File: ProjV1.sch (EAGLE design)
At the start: 24 parts, among them IC1 CD4007UBM, IC2 CD4007UBM, IC3 CD4007UBM, SW1 EC12E_SW, U1 MIC5504-3.3YM5-T5, U2 MCP2200-I/SS, U3 ATMEGA328PB-AU, Y1 12MHz

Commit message: Updated schematic and pdf
Switched serial chip to run on 3.3V and  updated the pdf file
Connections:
- removed net N$11: C1.2, U2.VSS
- removed net N$21: C1.1, U2.VUSB
- net +5V: no longer U2.VDD
- net 0: now also C1.2
- net VCC: now also C1.1, U2.VDD, U2.VUSB
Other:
- moved on the sheet: C1
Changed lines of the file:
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@@
 <part name="X_10" library="ngspice-simulation" library_urn="urn:adsk.eagle:library:527439" deviceset="GND" device=""/>
 <part name="P+6" library="supply1" library_urn="urn:adsk.eagle:library:371" deviceset="+5V" device=""/>
-<part name="P+7" library="supply1" library_urn="urn:adsk.eagle:library:371" deviceset="+5V" device=""/>
 <part name="P+8" library="supply1" library_urn="urn:adsk.eagle:library:371" deviceset="+5V" device=""/>
+<part name="X_11" library="ngspice-simulation" library_urn="urn:adsk.eagle:library:527439" deviceset="GND" device=""/>
+<part name="P+7" library="supply1" library_urn="urn:adsk.eagle:library:371" deviceset="VCC" device=""/>
 </parts>
 <sheets>
@@
 <instance part="X_2" gate="G$1" x="-241.3" y="337.82" smashed="yes"/>
 <instance part="X_3" gate="G$1" x="-226.06" y="261.62" smashed="yes"/>
-<instance part="C1" gate="G$1" x="-139.7" y="243.84" smashed="yes">
-<attribute name="NAME" x="-138.684" y="244.475" size="1.778" layer="95"/>
-<attribute name="VALUE" x="-138.684" y="239.649" size="1.778" layer="96"/>
+<instance part="C1" gate="G$1" x="-139.7" y="256.54" smashed="yes">
+<attribute name="NAME" x="-138.684" y="257.175" size="1.778" layer="95"/>
+<attribute name="VALUE" x="-138.684" y="252.349" size="1.778" layer="96"/>
 </instance>
 <instance part="X_4" gate="G$1" x="-71.12" y="223.52" smashed="yes"/>
@@
 <attribute name="VALUE" x="-231.14" y="355.6" size="1.778" layer="96" rot="R90"/>
 </instance>
-<instance part="P+7" gate="1" x="-139.7" y="271.78" smashed="yes">
-<attribute name="VALUE" x="-142.24" y="266.7" size="1.778" layer="96" rot="R90"/>
-</instance>
 <instance part="P+8" gate="1" x="-256.54" y="327.66" smashed="yes">
 <attribute name="VALUE" x="-259.08" y="322.58" size="1.778" layer="96" rot="R90"/>
+</instance>
+<instance part="X_11" gate="G$1" x="-139.7" y="246.38" smashed="yes"/>
+<instance part="P+7" gate="VCC" x="-139.7" y="271.78" smashed="yes">
+<attribute name="VALUE" x="-142.24" y="269.24" size="1.778" layer="96" rot="R90"/>
 </instance>
 </instances>
@@
 <junction x="-175.26" y="325.12"/>
 </segment>
-</net>
-<net name="N$21" class="0">
-<segment>
-<pinref part="U2" gate="G$1" pin="VUSB"/>
-<wire x1="-132.08" y1="261.62" x2="-139.7" y2="261.62" width="0.1524" layer="91"/>
-<pinref part="C1" gate="G$1" pin="1"/>
-<wire x1="-139.7" y1="261.62" x2="-139.7" y2="246.38" width="0.1524" layer="91"/>
+<segment>
+<pinref part="X_11" gate="G$1" pin="0"/>
+<pinref part="C1" gate="G$1" pin="2"/>
+<wire x1="-139.7" y1="246.38" x2="-139.7" y2="251.46" width="0.1524" layer="91"/>
 </segment>
 </net>
@@
 <pinref part="U$1" gate="G$1" pin="VCC"/>
 <wire x1="-63.5" y1="231.14" x2="-71.12" y2="231.14" width="0.1524" layer="91"/>
+</segment>
+<segment>
+<pinref part="U2" gate="G$1" pin="VDD"/>
+<wire x1="-132.08" y1="264.16" x2="-139.7" y2="264.16" width="0.1524" layer="91"/>
+<label x="-139.7" y="264.16" size="1.778" layer="95"/>
+<wire x1="-139.7" y1="269.24" x2="-139.7" y2="264.16" width="0.1524" layer="91"/>
+<pinref part="P+7" gate="VCC" pin="VCC"/>
+<pinref part="U2" gate="G$1" pin="VUSB"/>
+<wire x1="-132.08" y1="261.62" x2="-139.7" y2="261.62" width="0.1524" layer="91"/>
+<pinref part="C1" gate="G$1" pin="1"/>
+<wire x1="-139.7" y1="261.62" x2="-139.7" y2="259.08" width="0.1524" layer="91"/>
+<wire x1="-139.7" y1="264.16" x2="-139.7" y2="261.62" width="0.1524" layer="91"/>
+<junction x="-139.7" y="264.16"/>
+<junction x="-139.7" y="261.62"/>
 </segment>
 </net>
@@
 </segment>
 </net>
-<net name="N$11" class="0">
-<segment>
-<pinref part="U2" gate="G$1" pin="VSS"/>
-<wire x1="-132.08" y1="223.52" x2="-139.7" y2="223.52" width="0.1524" layer="91"/>
-<pinref part="C1" gate="G$1" pin="2"/>
-<wire x1="-139.7" y1="238.76" x2="-139.7" y2="223.52" width="0.1524" layer="91"/>
-</segment>
-</net>
 <net name="N$30" class="0">
 <segment>
@@
 </segment>
 <segment>
-<pinref part="U2" gate="G$1" pin="VDD"/>
-<wire x1="-132.08" y1="264.16" x2="-139.7" y2="264.16" width="0.1524" layer="91"/>
-<label x="-139.7" y="264.16" size="1.778" layer="95"/>
-<pinref part="P+7" gate="1" pin="+5V"/>
-<wire x1="-139.7" y1="269.24" x2="-139.7" y2="264.16" width="0.1524" layer="91"/>
-</segment>
-<segment>

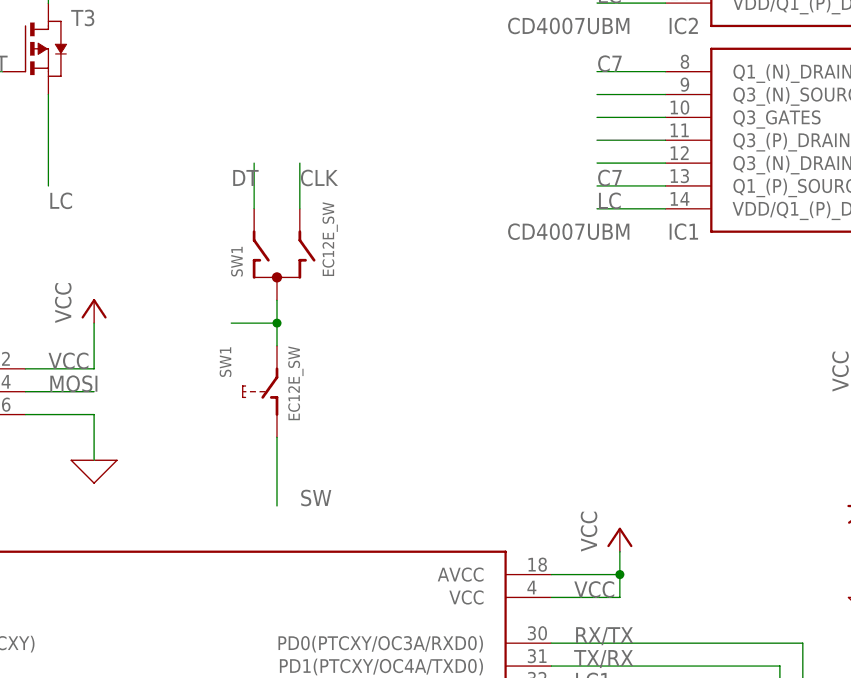
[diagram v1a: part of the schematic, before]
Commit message: Updated Board Layout and Cam filse
Rerouted wires to make board smaller
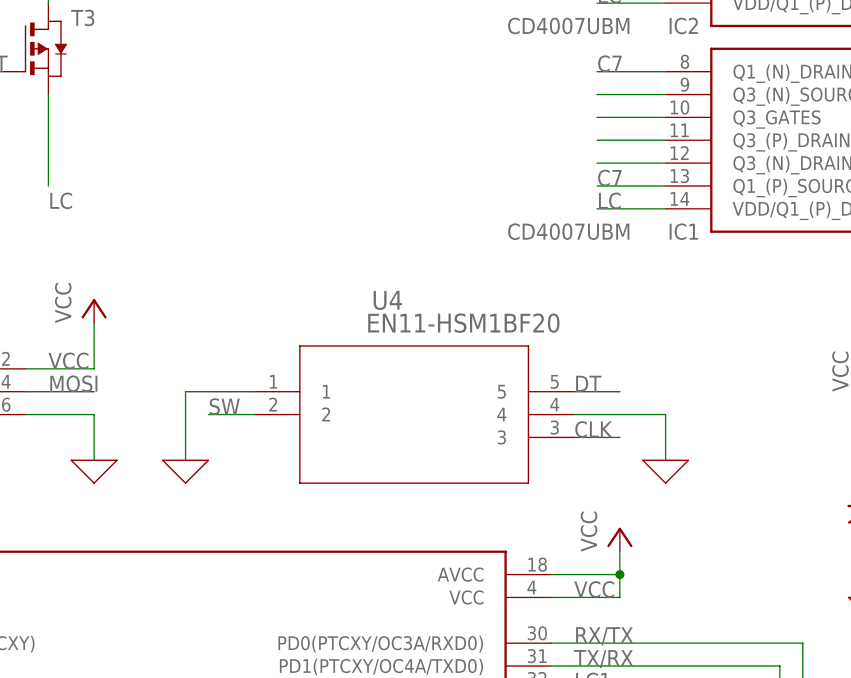
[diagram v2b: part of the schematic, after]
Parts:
- removed SW1: EC12E_SW, switch-alps:EC12E_SW
- added U4: EN11-HSM1BF20, EN11-HSM1BF20:EN11-HSM1BF20
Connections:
- removed net N$7: SW1G$1.C, SW1G$2.2
- net 0: now also U4.1, U4.4
- net CLK: now also U4.3; no longer SW1G$1.B
- net DT: now also U4.5; no longer SW1G$1.A
- net SW: now also U4.2; no longer SW1G$2.1
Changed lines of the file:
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@@
 <part name="LED4" library="led" library_urn="urn:adsk.eagle:library:259" deviceset="LED" device="CHIP-LED0805" package3d_urn="urn:adsk.eagle:package:15818/2"/>
 <part name="LED5" library="led" library_urn="urn:adsk.eagle:library:259" deviceset="LED" device="CHIP-LED0805" package3d_urn="urn:adsk.eagle:package:15818/2"/>
-<part name="SW1" library="switch-alps" library_urn="urn:adsk.eagle:library:373" deviceset="EC12E_SW" device="" package3d_urn="urn:adsk.eagle:package:27083/1"/>
 <part name="Y1" library="SparkFun-Clocks" deviceset="RESONATOR-16MHZ" device="SMD_3.2X1.3" value="12MHz"/>
 <part name="X_1" library="ngspice-simulation" library_urn="urn:adsk.eagle:library:527439" deviceset="GND" device=""/>
@@
 <part name="X_11" library="ngspice-simulation" library_urn="urn:adsk.eagle:library:527439" deviceset="GND" device=""/>
 <part name="P+7" library="supply1" library_urn="urn:adsk.eagle:library:371" deviceset="VCC" device=""/>
+<part name="U4" library="EN11-HSM1BF20" deviceset="EN11-HSM1BF20" device=""/>
+<part name="X_12" library="ngspice-simulation" library_urn="urn:adsk.eagle:library:527439" deviceset="GND" device=""/>
+<part name="X_13" library="ngspice-simulation" library_urn="urn:adsk.eagle:library:527439" deviceset="GND" device=""/>
 </parts>
 <sheets>
@@
 <attribute name="VALUE" x="-41.148" y="318.135" size="1.778" layer="96" rot="R180"/>
 </instance>
-<instance part="SW1" gate="G$1" x="-205.74" y="281.94" smashed="yes">
-<attribute name="PART" x="-209.55" y="281.94" size="1.27" layer="95" rot="R90"/>
-<attribute name="VALUE" x="-199.39" y="281.94" size="1.27" layer="96" rot="R90"/>
-</instance>
-<instance part="SW1" gate="G$2" x="-205.74" y="269.24" smashed="yes" rot="MR270">
-<attribute name="PART" x="-210.82" y="274.32" size="1.27" layer="95" rot="MR270"/>
-<attribute name="VALUE" x="-203.2" y="274.32" size="1.27" layer="96" rot="MR270"/>
-</instance>
 <instance part="Y1" gate="G$1" x="-83.82" y="251.46" smashed="yes" rot="MR270">
 <attribute name="NAME" x="-81.28" y="254.762" size="1.778" layer="95" font="vector" rot="MR270" align="center-right"/>
@@
 <attribute name="VALUE" x="-142.24" y="269.24" size="1.778" layer="96" rot="R90"/>
 </instance>
+<instance part="U4" gate="A" x="-210.82" y="269.24" smashed="yes">
+<attribute name="NAME" x="-195.2244" y="278.3586" size="2.0828" layer="95" ratio="6" rot="SR0"/>
+<attribute name="VALUE" x="-195.8594" y="275.8186" size="2.0828" layer="96" ratio="6" rot="SR0"/>
+</instance>
+<instance part="X_12" gate="G$1" x="-162.56" y="261.62" smashed="yes"/>
+<instance part="X_13" gate="G$1" x="-215.9" y="261.62" smashed="yes"/>
 </instances>
 <busses>
@@
 <wire x1="-139.7" y1="246.38" x2="-139.7" y2="251.46" width="0.1524" layer="91"/>
 </segment>
+<segment>
+<pinref part="X_12" gate="G$1" pin="0"/>
+<wire x1="-162.56" y1="261.62" x2="-162.56" y2="266.7" width="0.1524" layer="91"/>
+<pinref part="U4" gate="A" pin="4"/>
+<wire x1="-162.56" y1="266.7" x2="-172.72" y2="266.7" width="0.1524" layer="91"/>
+</segment>
+<segment>
+<pinref part="X_13" gate="G$1" pin="0"/>
+<wire x1="-215.9" y1="261.62" x2="-215.9" y2="269.24" width="0.1524" layer="91"/>
+<pinref part="U4" gate="A" pin="1"/>
+<wire x1="-208.28" y1="269.24" x2="-215.9" y2="269.24" width="0.1524" layer="91"/>
+</segment>
 </net>
 <net name="VCC" class="0">
@@
 </segment>
 </net>
-<net name="N$7" class="0">
-<segment>
-<pinref part="SW1" gate="G$2" pin="2"/>
-<pinref part="SW1" gate="G$1" pin="C"/>
-<wire x1="-205.74" y1="274.32" x2="-205.74" y2="276.86" width="0.1524" layer="91"/>
-<wire x1="-205.74" y1="276.86" x2="-205.74" y2="279.4" width="0.1524" layer="91"/>
-<wire x1="-205.74" y1="276.86" x2="-210.82" y2="276.86" width="0.1524" layer="91"/>
-<junction x="-205.74" y="276.86"/>
-</segment>
-</net>
 <net name="N$30" class="0">
 <segment>
@@
 <net name="DT" class="0">
 <segment>
-<pinref part="SW1" gate="G$1" pin="A"/>
-<wire x1="-208.28" y1="289.56" x2="-208.28" y2="294.64" width="0.1524" layer="91"/>
-<label x="-210.82" y="292.1" size="1.778" layer="95"/>
-</segment>
-<segment>
 <pinref part="U3" gate="G$1" pin="PC0(ADC0/PTCY/MISO1)"/>
 <wire x1="-261.62" y1="218.44" x2="-269.24" y2="218.44" width="0.1524" layer="91"/>
 <label x="-269.24" y="218.44" size="1.778" layer="95"/>
 </segment>
+<segment>
+<pinref part="U4" gate="A" pin="5"/>
+<wire x1="-172.72" y1="269.24" x2="-167.64" y2="269.24" width="0.1524" layer="91"/>
+<label x="-172.72" y="269.24" size="1.778" layer="95"/>
+</segment>
 </net>
 <net name="CLK" class="0">
-<segment>
-<pinref part="SW1" gate="G$1" pin="B"/>
-<wire x1="-203.2" y1="289.56" x2="-203.2" y2="294.64" width="0.1524" layer="91"/>
-<label x="-203.2" y="292.1" size="1.778" layer="95"/>
-</segment>
 <segment>
 <pinref part="U3" gate="G$1" pin="PB0(ICP1/CLKO/PTCXY)"/>
@@
 <label x="-269.24" y="241.3" size="1.778" layer="95"/>
 </segment>
+<segment>
+<pinref part="U4" gate="A" pin="3"/>
+<wire x1="-172.72" y1="264.16" x2="-167.64" y2="264.16" width="0.1524" layer="91"/>
+<label x="-172.72" y="264.16" size="1.778" layer="95"/>
+</segment>
 </net>
 <net name="SW" class="0">
-<segment>
-<pinref part="SW1" gate="G$2" pin="1"/>
-<wire x1="-205.74" y1="264.16" x2="-205.74" y2="256.54" width="0.1524" layer="91"/>
-<label x="-203.2" y="256.54" size="1.778" layer="95"/>
-</segment>
 <segment>
 <pinref part="U3" gate="G$1" pin="PD7(PTCXY/AIN1)"/>
@@
 <label x="-172.72" y="223.52" size="1.778" layer="95"/>
 </segment>
-</net>
+<segment>
+<pinref part="U4" gate="A" pin="2"/>
+<wire x1="-208.28" y1="266.7" x2="-213.36" y2="266.7" width="0.1524" layer="91"/>
+<label x="-213.36" y="266.7" size="1.778" layer="95"/>
+</segment>
+</net>
